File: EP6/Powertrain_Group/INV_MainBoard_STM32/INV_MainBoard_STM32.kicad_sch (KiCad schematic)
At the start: 36 parts, among them J1 FX26-30P-1SV, J10 CAN, J11 CAN, J12 CAN, J16 SPI, J2 motorSense, J7 phase control monitor, J8 current, J9 CAN, Q1 2N7002, Q2 2N7002

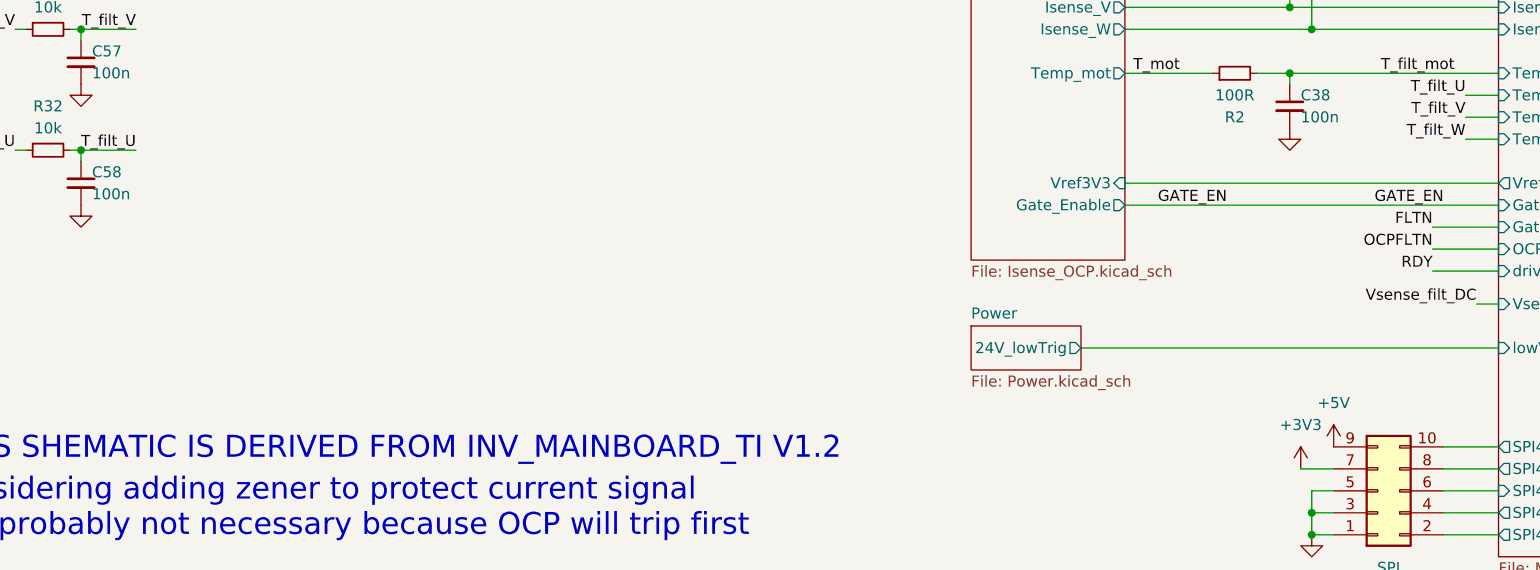
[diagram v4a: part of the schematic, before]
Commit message: add comments to INV boards after testing JLC PCBs
INV boards included:
INV_GateDriver: mainly about QSPI SPRAM
INV_MainBoard_STM32: mainly about mistake VINC of LM26420
INV_MainBoard_TI: mainly about trace too long and incorrect spec of Rg
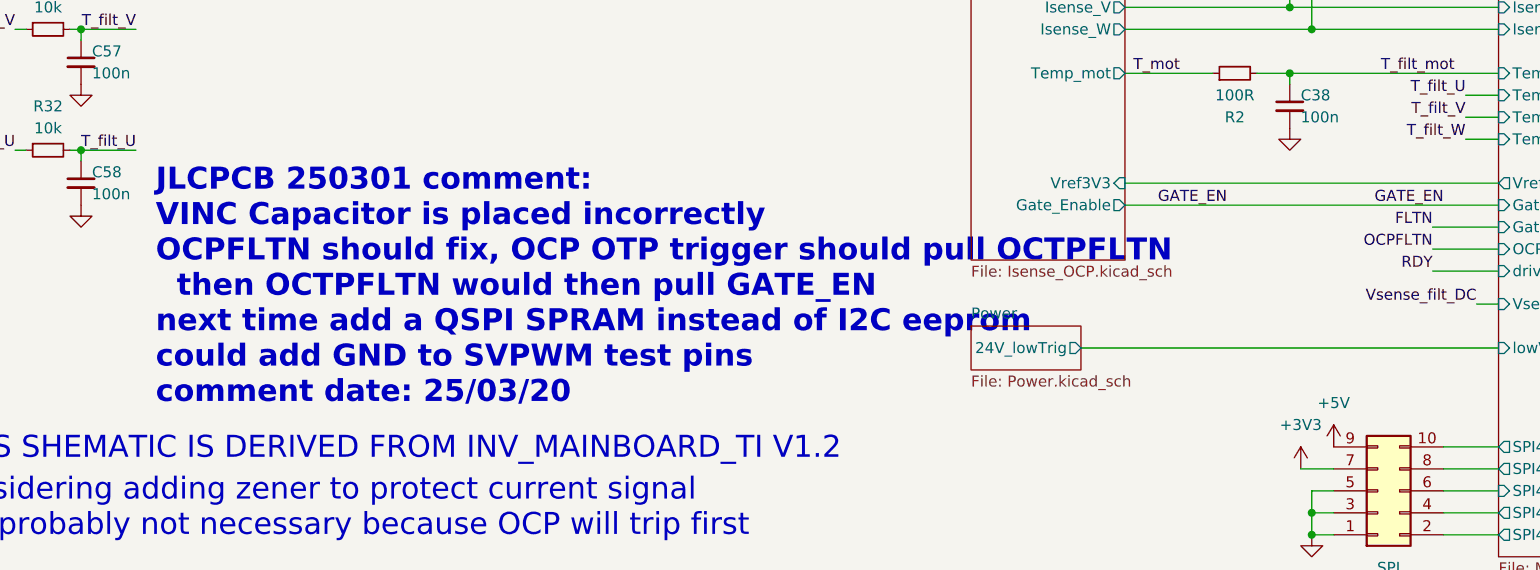
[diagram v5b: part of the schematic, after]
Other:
- note added: "JLCPCB 250301 comment: VINC Capacitor is placed incorrectly OCPFLTN should fix, OCP OTP trigger should pull OCTPFLTN then OCTPFLTN would then pull GATE_EN next time add a QSPI SPRAM instead of I2C eeprom could add GND to SVPWM test pins comment date: 25/03/20"
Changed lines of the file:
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@@
+		)
+	)
+	(text "JLCPCB 250301 comment:\nVINC Capacitor is placed incorrectly\nOCPFLTN should fix, OCP OTP trigger should pull OCTPFLTN\n  then OCTPFLTN would then pull GATE_EN\nnext time add a QSPI SPRAM instead of I2C eeprom\ncould add GND to SVPWM test pins\ncomment date: 25/03/20"
+		(exclude_from_sim no)
+		(at 44.196 71.882 0)
+		(effects
+			(font
+				(size 2.54 2.54)
+				(thickness 0.508)
+				(bold yes)
+				(color 255 0 0 1)
+			)
+			(justify left top)
 		)
 	)

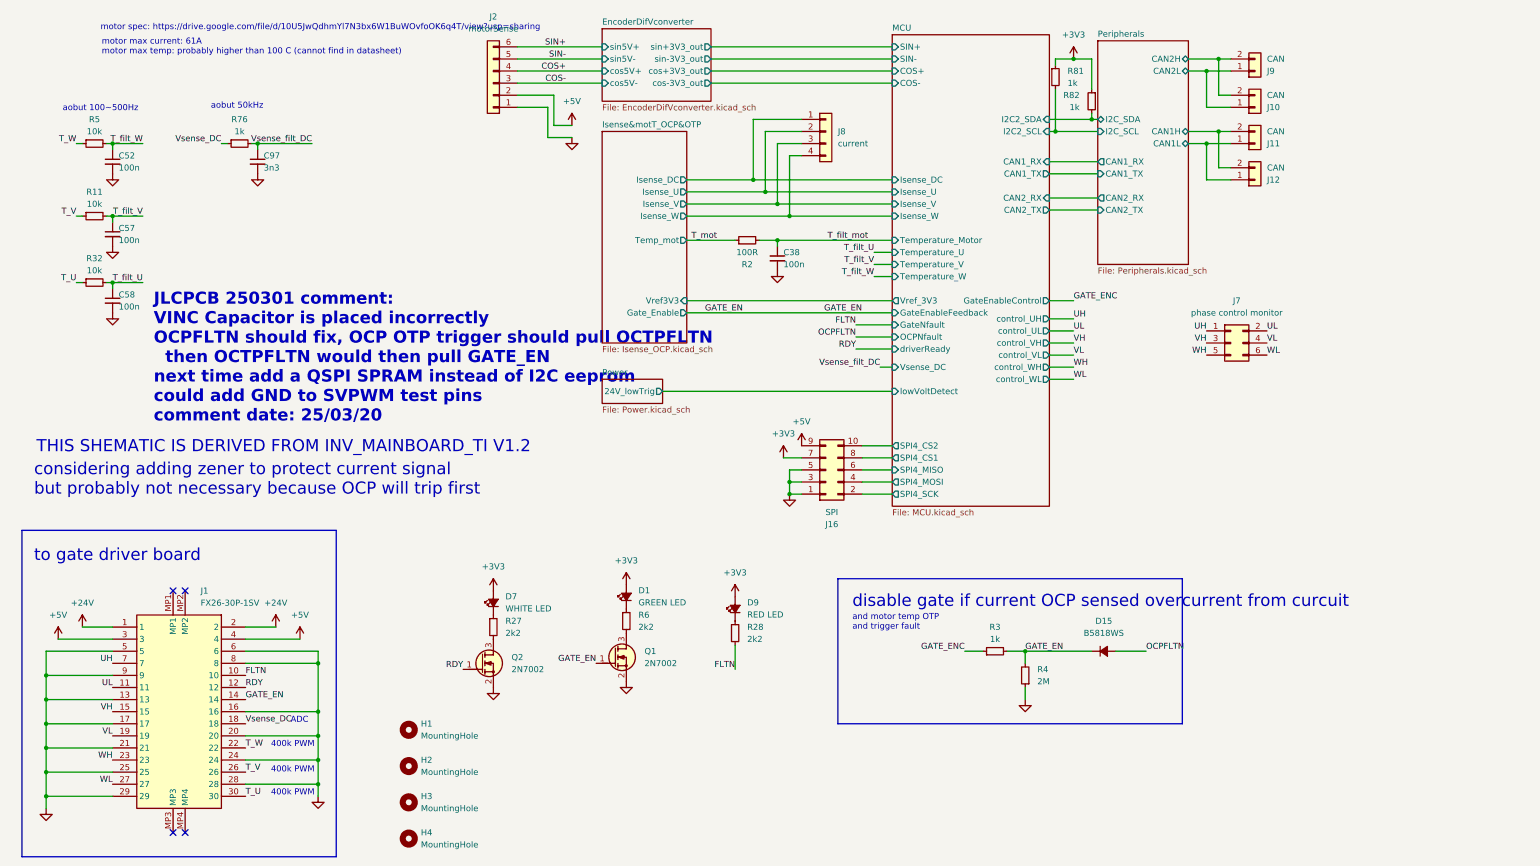
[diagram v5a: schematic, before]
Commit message: update INV_MainBoard_STM32 to V3.0
PCB: INV_MainBoard_STM32 V3.0
V3.0 remove low volte trig
     add RC filt for OCP, OTP
     dedicated OTP, OCP pull down gate enable
     pending: fault hardware OTP/OCP latch
     pending: add QSPI DRAM
     use JST PH
     exterinal pull up for flt, ready
     fix CAN1, 2 label on board
     use 1k, 2k for encoder divider
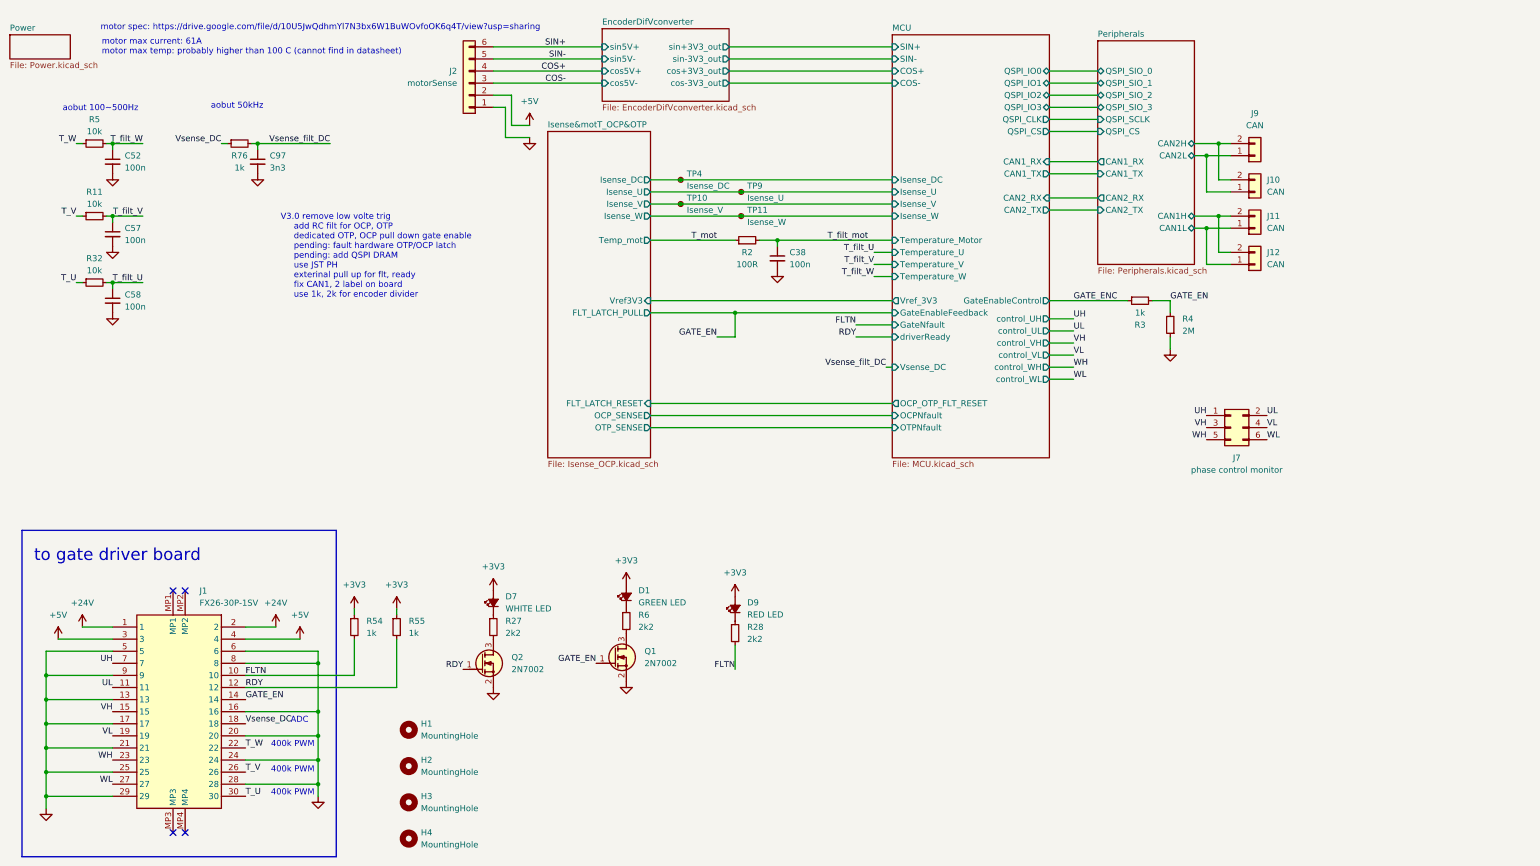
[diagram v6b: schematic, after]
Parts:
- removed D15: B5818WS, Diode_SMD:D_SOD-323, symbol Device:D_Small_Filled
- removed J16: SPI, Connector_PinHeader_2.54mm:PinHeader_2x05_P2.54mm_Vertical, symbol Connector_Generic:Conn_02x05_Odd_Even
- removed J8: current, Connector_PinHeader_2.54mm:PinHeader_1x04_P2.54mm_Vertical, symbol Connector_Generic:Conn_01x04
- removed R81, R82: 1k, Resistor_SMD:R_0402_1005Metric, symbol Device:R_Small
- added R54, R55: 1k, Resistor_SMD:R_0402_1005Metric, symbol Device:R_Small
- added TP10: Isense_V, TestPoint:TestPoint_Pad_D1.0mm, symbol Connector:TestPoint_Small
- added TP11: Isense_W, TestPoint:TestPoint_Pad_D1.0mm, symbol Connector:TestPoint_Small
- added TP4: Isense_DC, TestPoint:TestPoint_Pad_D1.0mm, symbol Connector:TestPoint_Small
- added TP9: Isense_U, TestPoint:TestPoint_Pad_D1.0mm, symbol Connector:TestPoint_Small
- J2: footprint Connector_JST:JST_XH_B6B-XH-A_1x06_P2.50mm_Vertical -> Connector_JST:JST_PH_B6B-PH-K_1x06_P2.00mm_Vertical
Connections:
- net +3V3: now also R54.1, R55.1
- net FLTN: now also R54.2
- net Isense&motT_OCP&OTP/Isense_DC: now also TP4.1
- net Isense&motT_OCP&OTP/Isense_U: now also TP9.1
- net Isense&motT_OCP&OTP/Isense_V: now also TP10.1
- net Isense&motT_OCP&OTP/Isense_W: now also TP11.1
- net RDY: now also R55.2
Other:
- sheet Isense&motT_OCP&OTP ports: added FLT_LATCH_PULL, FLT_LATCH_RESET, OCP_SENSE, OTP_SENSE; removed Gate_Enable
- sheet MCU ports: added OCP_OTP_FLT_RESET, OTPNfault, QSPI_CLK, QSPI_CS, QSPI_IO0, QSPI_IO1, QSPI_IO2, QSPI_IO3; removed I2C2_SCL, I2C2_SDA, SPI4_CS1, SPI4_CS2, SPI4_MISO, SPI4_MOSI, SPI4_SCK, lowVoltDetect
- sheet Peripherals ports: added QSPI_CS, QSPI_SCLK, QSPI_SIO_0, QSPI_SIO_1, QSPI_SIO_2, QSPI_SIO_3; removed I2C_SCL, I2C_SDA
- sheet Power ports: added none; removed 24V_lowTrig
- note added: "V3.0 remove low volte trig add RC filt for OCP, OTP dedicated OTP, OCP pull down gate enable pending: fault hardware OTP/OCP latch pending: add QSPI DRAM use JST PH exterinal pull up for flt, ready fix CAN1, 2 label on board use 1k, 2k for encoder divider"
- note removed: "JLCPCB 250301 comment: VINC Capacitor is placed incorrectly OCPFLTN should fix, OCP OTP trigger should pull OCTPFLTN then OCTPFLTN would then pull GATE_EN next time add a QSPI SPRAM instead of I2C eeprom could add GND to SVPWM test pins comment date: 25/03/20"
- note removed: "THIS SHEMATIC IS DERIVED FROM INV_MAINBOARD_TI V1.2"
- note removed: "and motor temp OTP"
- note removed: "and trigger fault"
- note removed: "considering adding zener to protect current signal but probably not necessary because OCP will trip first"
- note removed: "disable gate if current OCP sensed overcurrent from curcuit"
- moved on the sheet: J10, J11, J12, J2, J7, J9, R3, R4

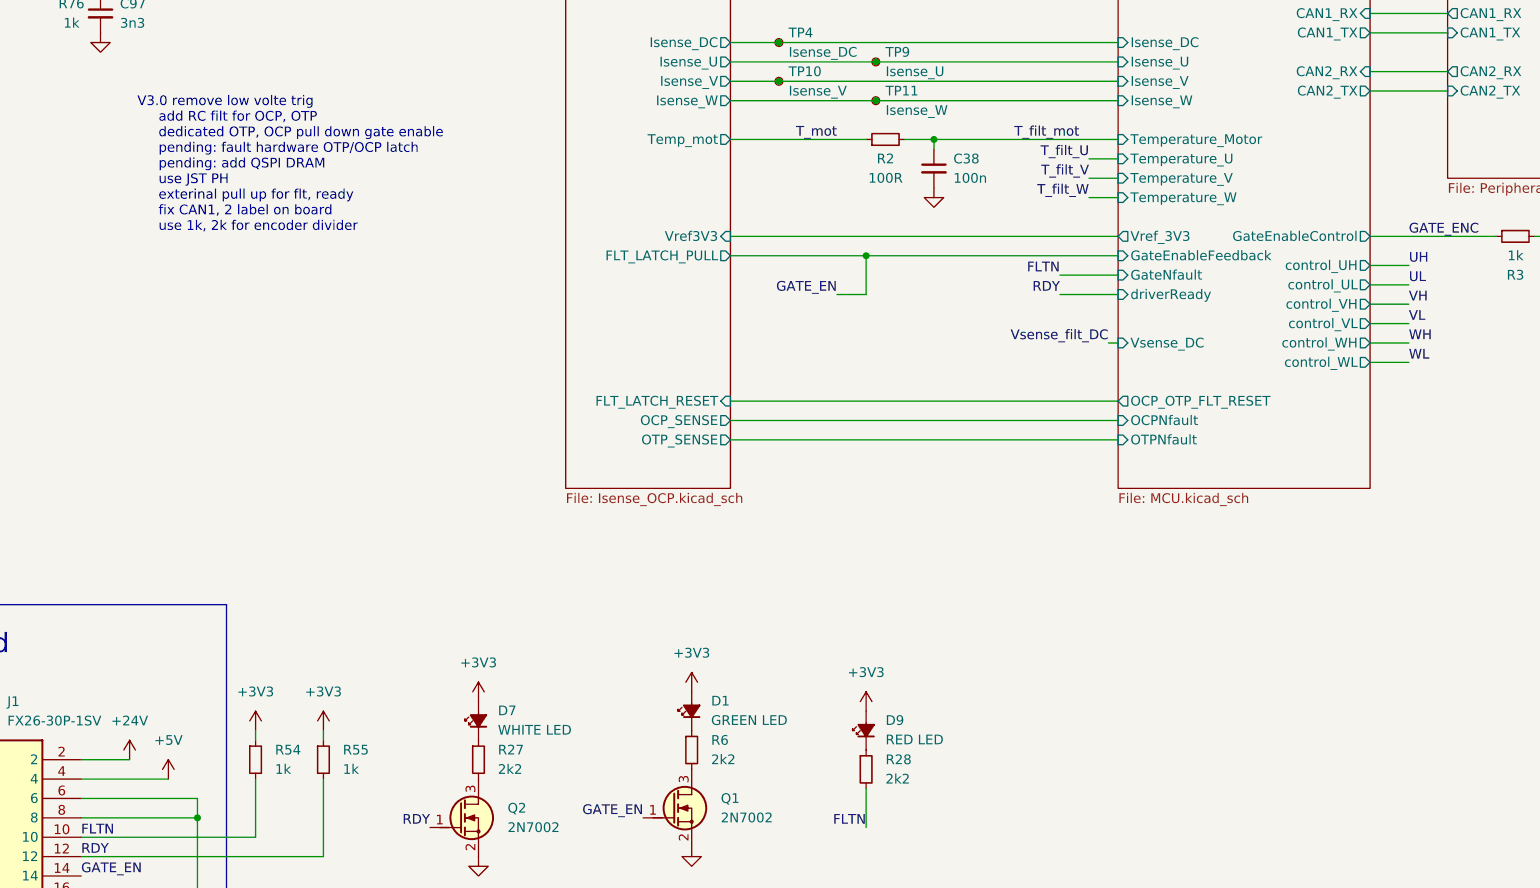
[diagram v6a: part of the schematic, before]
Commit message: update INV_MainBoard_STM32 to V3.1
V3.1 fix R93 to 100R
     add led for OCP, OTP flt
     add default Res for OTP threshold
     add gnd pins for testing
     fix latch circuit
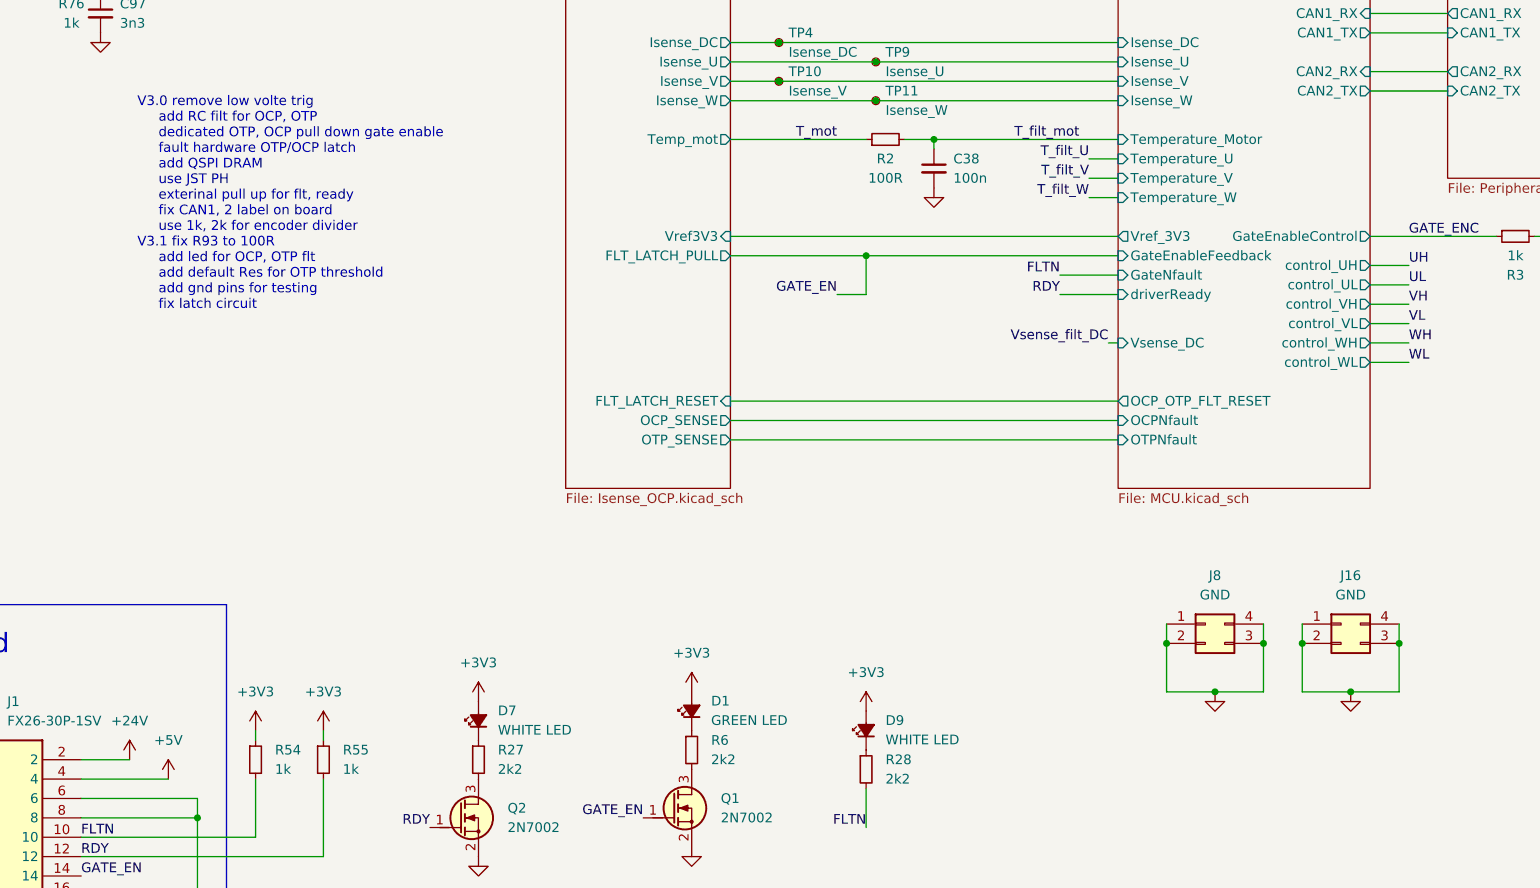
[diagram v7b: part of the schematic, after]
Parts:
- added J16, J8: GND, Connector_PinHeader_2.54mm:PinHeader_2x02_P2.54mm_Vertical, symbol Connector_Generic:Conn_02x02_Counter_Clockwise
- D9: value RED LED -> WHITE LED
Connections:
- net GND: now also J16.1 (Pin_1), J16.2 (Pin_2), J16.3 (Pin_3), J16.4 (Pin_4), J8.1 (Pin_1), J8.2 (Pin_2), J8.3 (Pin_3), J8.4 (Pin_4)
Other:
- note added: "V3.0 remove low volte trig add RC filt for OCP, OTP dedicated OTP, OCP pull down gate enable fault hardware OTP/OCP latch add QSPI DRAM use JST PH exterinal pull up for flt, ready fix CAN1, 2 label on board use 1k, 2k for encoder divider V3.1 fix R93 to 100R add led for OCP, OTP flt add default Res for OTP threshold add gnd pins for testing fix latch circuit"
- note removed: "V3.0 remove low volte trig add RC filt for OCP, OTP dedicated OTP, OCP pull down gate enable pending: fault hardware OTP/OCP latch pending: add QSPI DRAM use JST PH exterinal pull up for flt, ready fix CAN1, 2 label on board use 1k, 2k for encoder divider"
